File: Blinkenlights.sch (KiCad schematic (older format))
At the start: 80 parts, among them J1 PDI, U1 ATXMEGA8E5-MU

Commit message: Squiggles! Silk!
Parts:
- renumbered C7 to C801, C8 to C802, DS1 to DS801, DS2 to DS802, DS3 to DS803, DS4 to DS804, DS5 to DS805, DS6 to DS806, DS7 to DS807, DS8 to DS808, DS9 to DS809, DS10 to DS810, DS11 to DS811, DS12 to DS812, DS13 to DS813, DS14 to DS814, DS15 to DS815, DS16 to DS816, DS17 to DS817, DS18 to DS818, DS23 to DS819, DS24 to DS820, DS25 to DS821, DS26 to DS822, DS27 to DS823, DS28 to DS824, DS29 to DS825, DS30 to DS826, DS31 to DS827, DS32 to DS828, DS33 to DS829, DS34 to DS830, DS35 to DS831, DS36 to DS832, DS37 to DS833, DS38 to DS834, DS39 to DS835, DS40 to DS836, DS41 to DS837, DS42 to DS838, DS43 to DS839, DS44 to DS840, DS45 to DS841, DS46 to DS842, DS47 to DS843, DS48 to DS844, DS49 to DS845, DS50 to DS846, DS51 to DS847, DS52 to DS848, DS53 to DS849, DS54 to DS850, DS55 to DS851, DS56 to DS852, DS57 to DS853, DS58 to DS854, DS59 to DS855, DS60 to DS856, DS61 to DS857, DS62 to DS858, DS63 to DS859, J1 to J801, R5 to R801, R6 to R802, R7 to R803, R10 to R804, R11 to R805, R12 to R806, R13 to R807, R15 to R808, R16 to R809, R18 to R810, R19 to R811, R20 to R812, R21 to R813, R50 to R814, R51 to R815, R53 to R816, R54 to R817, U1 to U801

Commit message: Final BOM
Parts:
- C801, C802: value 100n -> 1u; BOM CAP MLCC 100n ≥X5R 25V 10% [0402] -> CAP MLCC 1u 6.3V 20% [0402]
- R803: value 51k -> 4k3; BOM RES SMD 51k 1% [0402] -> RES SMD 4k3 [0402]
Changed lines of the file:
@@
 AR Path="/577C2AEA/577B8E2D" Ref="C801"  Part="1"
 F 0 "C801" H 1437 6604 50  0000 R CNN
-F 1 "100n" H 1437 6695 50  0000 R CNN
+F 1 "1u" H 1437 6695 50  0000 R CNN
 F 2 "IPC7351-Nominal:CAPC1005X55" H 1550 6650 50  0001 C CNN
 F 3 "" H 1540 6625 60  0000 C CNN
-F 4 "CAP MLCC 100n ≥X5R 25V 10% [0402]" H 2350 7200 60  0001 C CNN "BOM"
+F 4 "CAP MLCC 1u 6.3V 20% [0402]" H 2350 7200 60  0001 C CNN "BOM"
 	1    1550 6650
 	-1   0    0    1
@@
 AR Path="/577C2AEA/577B942B" Ref="C802"  Part="1"
 F 0 "C802" H 1837 6604 50  0000 R CNN
-F 1 "100n" H 1837 6695 50  0000 R CNN
+F 1 "1u" H 1837 6695 50  0000 R CNN
 F 2 "IPC7351-Nominal:CAPC1005X55" H 1950 6650 50  0001 C CNN
 F 3 "" H 1940 6625 60  0000 C CNN
-F 4 "CAP MLCC 100n ≥X5R 25V 10% [0402]" H 2750 7200 60  0001 C CNN "BOM"
+F 4 "CAP MLCC 1u 6.3V 20% [0402]" H 2750 7200 60  0001 C CNN "BOM"
 	1    1950 6650
 	-1   0    0    1
@@
 P 2300 7250
 F 0 "R803" H 2237 7204 50  0000 R CNN
-F 1 "51k" H 2237 7295 50  0000 R CNN
+F 1 "4k3" H 2237 7295 50  0000 R CNN
 F 2 "IPC7351-Nominal:RESC1005X40" H 2300 7250 50  0001 C CNN
 F 3 "" H 2300 7300 60  0000 C CNN
-F 4 "RES SMD 51k 1% [0402]" H 3050 7800 60  0001 C CNN "BOM"
+F 4 "RES SMD 4k3 [0402]" H 3050 7800 60  0001 C CNN "BOM"
 	1    2300 7250
 	-1   0    0    1

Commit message: Switch LED metrix driver
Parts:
- removed C801: 1u, IPC7351-Nominal:CAPC1005X55, symbol C-0402
- removed DS825: BRG_P1V2(R), smd-semi:LED-0603, symbol LED-0603
- removed DS826: CPU_P1V2(R), smd-semi:LED-0603, symbol LED-0603
- removed DS827: BRG_P1V2(G), smd-semi:LED-0603, symbol LED-0603
- removed DS828: CPU_P1V2(G), smd-semi:LED-0603, symbol LED-0603
- removed DS829: PCI_N12(R), smd-semi:LED-0603, symbol LED-0603
- removed DS830: MEM_PV75(R), smd-semi:LED-0603, symbol LED-0603
- removed DS831: PCI_N12(G), smd-semi:LED-0603, symbol LED-0603
- removed DS832: MEM_PV75(G), smd-semi:LED-0603, symbol LED-0603
- removed J801: PDI, conn-100mil:CONN-100MIL-M-2x3, symbol CONN-100MIL-M-2x3
- removed R803: 4k3, IPC7351-Nominal:RESC1005X40, symbol R-0402
- removed R804, R807, R808, R811, R812, R814, R815: 750, IPC7351-Nominal:RESC1005X40, symbol R-0402
- removed R805, R806, R809, R810, R813, R816, R817: 300, IPC7351-Nominal:RESC1005X40, symbol R-0402
- removed U801: ATXMEGA8E5-MU, IPC7351-Nominal:QFN50P500X500X100-33, symbol ATXMEGA8E5-MU
- added C801: 10u, IPC7351-Nominal:CAPMP3528X210, symbol C-TANT-AVX-B
- added C803, C804: 1u, IPC7351-Nominal:CAPC1005X55, symbol C-0402
- added U801: AS1130-BTST, IPC7351-Nominal:SOP65P640X120-28, symbol AS1130-BTST
- C802: BOM CAP MLCC 1u 6.3V 20% [0402] -> DIST DIGIKEY 490-6281-1-ND
- DS801: value PCI_P12(R) -> P12V_PCI(R)
- DS802: value PCI_P12(G) -> P5V_PCI_A(R); BOM LED GREEN [0603] -> LED RED [0603]
- DS803: value PCI_P5(R) -> P5V_PCI_B(R)
- DS804: value BRG_P5(R) -> P3V3_PCI_A(R)
- DS805: value CPU_P5(R) -> P3V3_PCI_B(R)
- DS806: value PCI_P5(G) -> N12V_PCI(R); BOM LED GREEN [0603] -> LED RED [0603]
- DS807: value BRG_P5(G) -> P12V_PCI(G)
- DS808: value CPU_P5(G) -> P5V_PCI_A(G)
- DS809: value PCI_P3V3(R) -> P5V_PCI_B(G); BOM LED RED [0603] -> LED GREEN [0603]
- DS810: value BRG_P3V3(R) -> P3V3_PCI_A(G); BOM LED RED [0603] -> LED GREEN [0603]
- DS811: value CPU_P3V3(R) -> P3V3_PCI_B(G); BOM LED RED [0603] -> LED GREEN [0603]
- DS812: value AUX_P3V3(R) -> N12V_PCI(G); BOM LED RED [0603] -> LED GREEN [0603]
- DS813: value SBY_P3V3(R) -> P3V3_STBY(R)
- DS814: value PCI_P3V3(G) -> P3V3_AUX(R); BOM LED GREEN [0603] -> LED RED [0603]
- DS815: value BRG_P3V3(G) -> P3V3_LOGIC(R); BOM LED GREEN [0603] -> LED RED [0603]
- DS816: value CPU_P3V3(G) -> P1V5_LOGIC(R); BOM LED GREEN [0603] -> LED RED [0603]
- DS817: value AUX_P3V3(G) -> P1V2_LOGIC(R); BOM LED GREEN [0603] -> LED RED [0603]
- DS818: value SBY_P3V3(G) -> PV75_TERM(R); BOM LED GREEN [0603] -> LED RED [0603]
- DS819: value BRG_P1V5(R) -> P3V3_STBY(G); BOM LED RED [0603] -> LED GREEN [0603]
- DS820: value MEM_P1V5(R) -> P3V3_AUX(G); BOM LED RED [0603] -> LED GREEN [0603]
- DS821: value CPU_P1V5(R) -> P3V3_LOGIC(G); BOM LED RED [0603] -> LED GREEN [0603]
- DS822: value BRG_P1V5(G) -> P1V5_LOGIC(G)
- DS823: value MEM_P1V5(G) -> P1V2_LOGIC(G)
- DS824: value CPU_P1V5(G) -> PV75_TERM(G)
- R801: value 750 -> 0R; BOM RES SMD 750 1% [0402] -> RES SMD 0R [0402]
- R802: value 300 -> 0R; BOM RES SMD 300 1% [0402] -> RES SMD 0R [0402]
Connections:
- net labels added: CS0, CS1, CS10, CS11, CS2, CS3, CS4, CS5, CS6, CS7, CS8, CS9
- net labels removed: COL0, COL1, COL10, COL11, COL12, COL13, COL14, COL15, COL2, COL3, COL4, COL5, COL6, COL7, COL8, COL9, ROW0, ROW1, ROW2, ROW3, ROW4, ROW5, ROW6, ROW7
- wire segments 267 -> 215
- no-connect marks 5 -> 2
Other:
- note added: "0x00"
- note added: "0x01"
- note added: "0x02"
- note added: "0x03"
- note added: "0x04"
- note added: "0x10"
- note added: "0x11"
- note added: "0x12"
- note added: "0x13"
- note added: "0x14"
- note added: "0x20"
- note added: "0x21"
- note added: "0x23"
- note added: "0x25"
- note added: "0x30"
- note added: "0x31"
- note added: "0x32"
- note added: "0x33"
- note added: "0x34"
- note added: "0x40"
- note added: "0x41"
- note added: "0x42"
- note added: "0x43"
- note added: "0x44"
- note added: "0x50"
- note added: "0x51"
- note added: "0x52"
- note added: "0x53"
- note added: "0x54"
- note added: "0x70"
- note added: "0x71"
- note added: "0x72"
- note added: "0x73"
- note added: "0x74"
- note added: "0x75"
- note added: "0x80"
- note added: "0x81"
- note added: "0x82"
- note added: "0x83"
- note added: "0x84"
- note added: "0x85"
- note added: "0x90"
- note added: "0x91"
- note added: "0x92"
- note added: "0x93"
- note added: "0x94"
- note added: "0x95"
- note added: "0xA2"
- note added: "0xB1"
- note added: "0xB2"
- note added: "ADDR: 0x37"
- note removed: "I2C: 0x57"
- note removed: "LEDs:\nGreen: LG L29K-F2J1-24, current = 5mA, Vf=1.8V\nRed: LS Q976-NR-1, current = 2mA, Vf=1.8V"

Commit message: Rearrange LEDs a bit, switch to al-poly caps
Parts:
- DS833: value POWER(R) -> ECFW(R)
- DS834: value CARD(R) -> POWER(R)
- DS835: value BIT(R) -> CARD(R)
- DS836: value CLK(R) -> BIT(R)
- DS839: value POWER(G) -> ECFW(G)
- DS840: value CARD(G) -> POWER(G)
- DS841: value BIT-BR(G) -> CARD(G)
- DS842: value CLK(G) -> BIT(G)
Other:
- moved on the sheet: DS845, DS846

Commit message: Fix more shit for to pass ERC
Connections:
- no-connect marks 2 -> 3

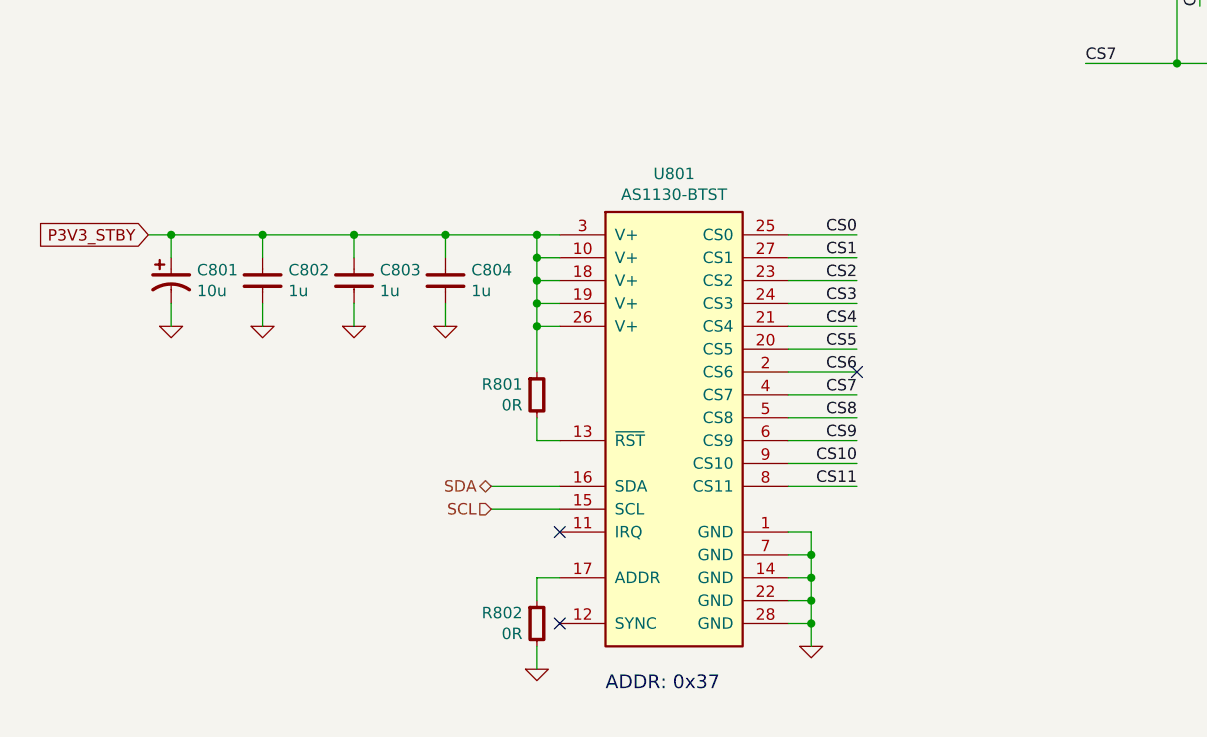
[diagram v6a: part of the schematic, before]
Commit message: Tidy schematics and produce PDF
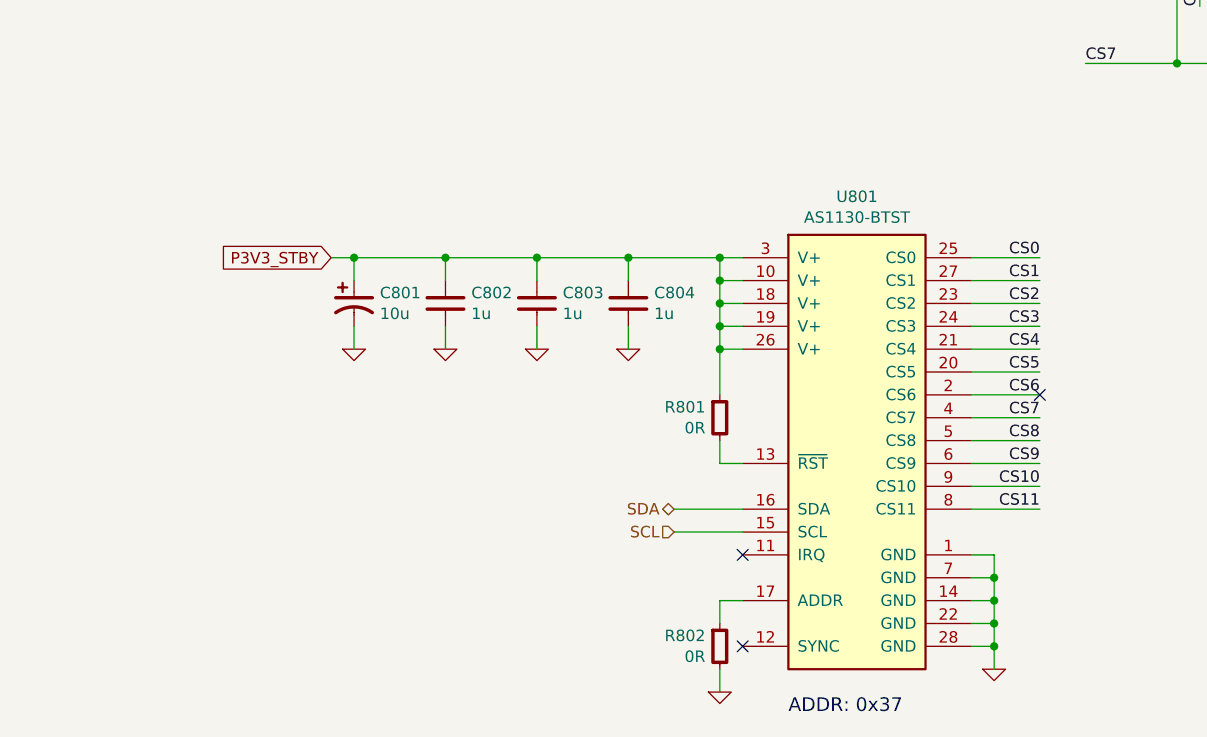
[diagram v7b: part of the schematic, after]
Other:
- moved on the sheet: C801, C802, C803, C804, R801, R802, U801

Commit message: Update for KiCad 5
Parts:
- C801: symbol C-TANT-AVX-B -> pasv-cap:C-TANT-AVX-B
- C802, C803, C804: symbol C-0402 -> pasv-cap:C-0402
- DS801, DS802, DS803, DS804, DS805, DS806, DS807, DS808, DS809, DS810, DS811, DS812, DS813, DS814, DS815, DS816, DS817, DS818, DS819, DS820, DS821, DS822, DS823, DS824, DS833, DS834, DS835, DS836, DS837, DS838, DS839, DS840, DS841, DS842, DS843, DS844, DS845, DS846, DS847, DS848, DS849, DS850, DS851, DS852, DS853, DS854, DS855, DS856, DS857, DS858, DS859: symbol LED-0603 -> semi-opto-generic:LED-0603
- R801, R802: symbol R-0402 -> pasv-res:R-0402
- U801: symbol AS1130-BTST -> AMS:AS1130-BTST
